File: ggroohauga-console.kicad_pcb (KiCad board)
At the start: 2 copper layers, 95 x 31 mm, 6 parts

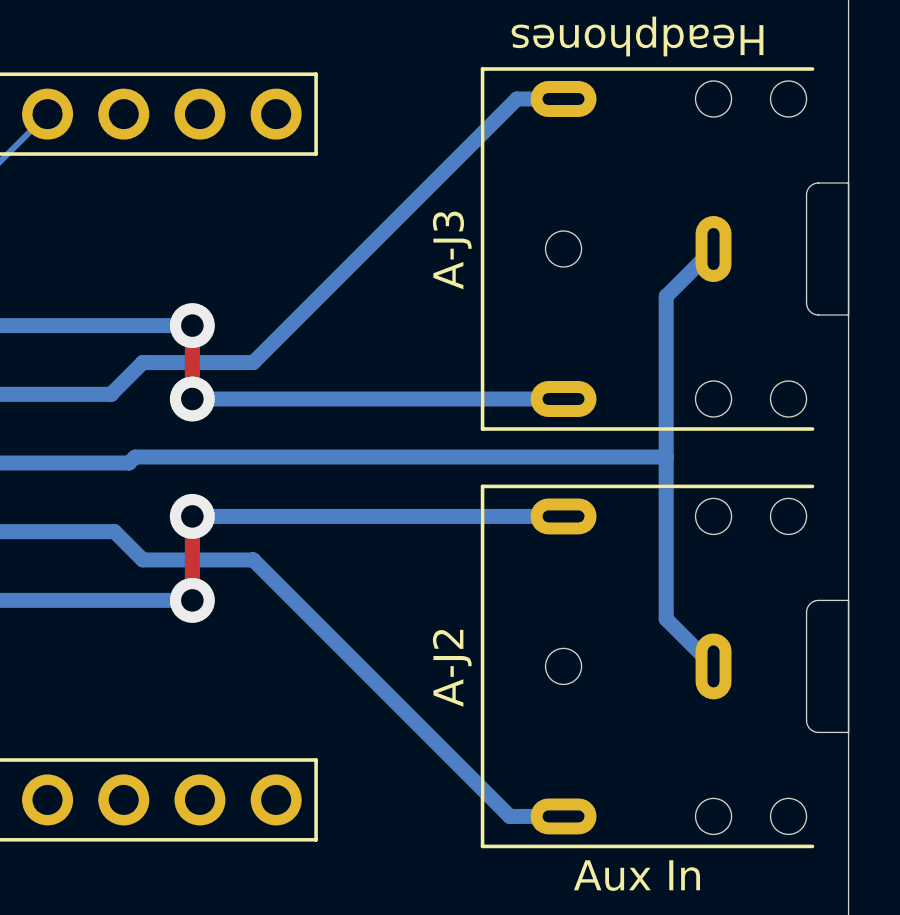
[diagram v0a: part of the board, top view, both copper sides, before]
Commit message: Fix component references for audio jacks
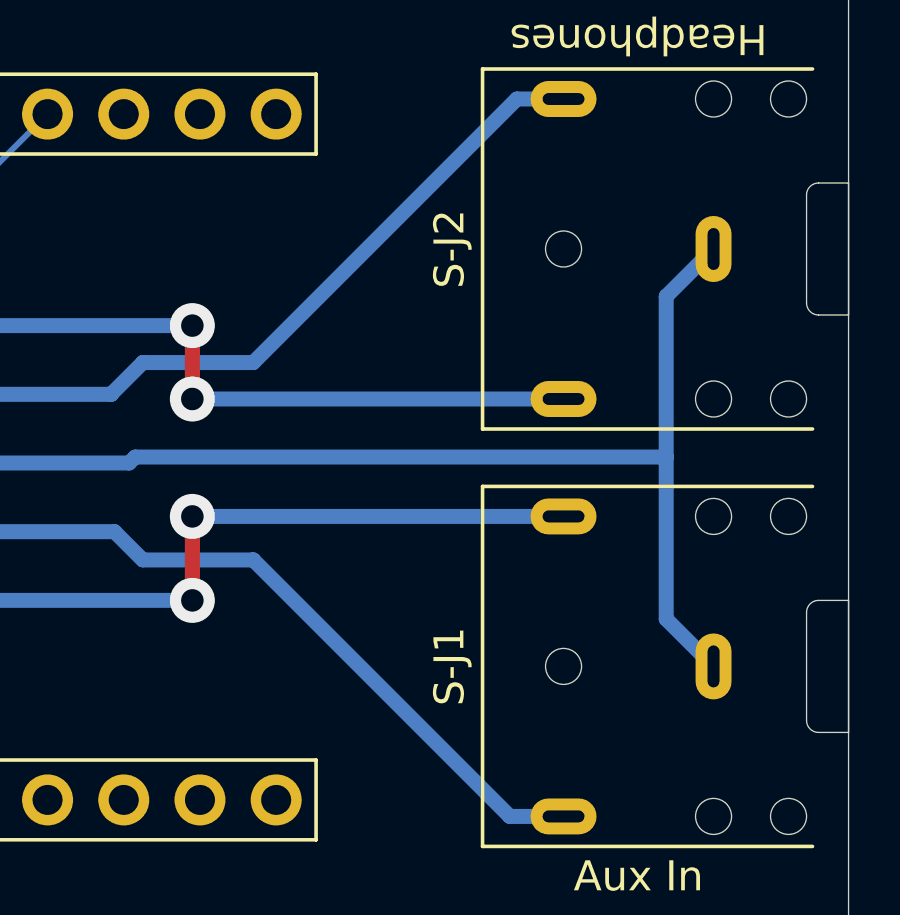
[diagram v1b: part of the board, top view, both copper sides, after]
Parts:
- renumbered A-J2 to S-J1, A-J3 to S-J2
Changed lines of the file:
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@@
 		(descr "TRS 3.5mm, horizontal, through-hole, https://www.cuidevices.com/product/resource/pdf/sj1-352xn.pdf")
 		(tags "TRS audio jack stereo horizontal")
-		(property "Reference" "A-J2"
+		(property "Reference" "S-J1"
 			(at 0 -8.8 90)
 			(layer "F.SilkS")
@@
 		(descr "TRS 3.5mm, horizontal, through-hole, https://www.cuidevices.com/product/resource/pdf/sj1-352xn.pdf")
 		(tags "TRS audio jack stereo horizontal")
-		(property "Reference" "A-J3"
+		(property "Reference" "S-J2"
 			(at 0 -8.8 90)
 			(layer "F.SilkS")

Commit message: Add "music with rocks in" image
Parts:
- added MUSICWITHROCKSIN: LOGO, LOGO, B.Cu at (81.3, 64.5)

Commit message: Fix thin lines in image
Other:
- board text added: "https://github.com/nomis/ggroohauga-pcb (console)"
- board text added: "urn:oid:1.3.6.1.4.1.39777.1.3.1.2.3"
- board text removed: "urn:oid:1.3.6.1.4.1.39777.1.3.1.2.3 https://github.com/nomis/ggroohauga-pcb (console)"

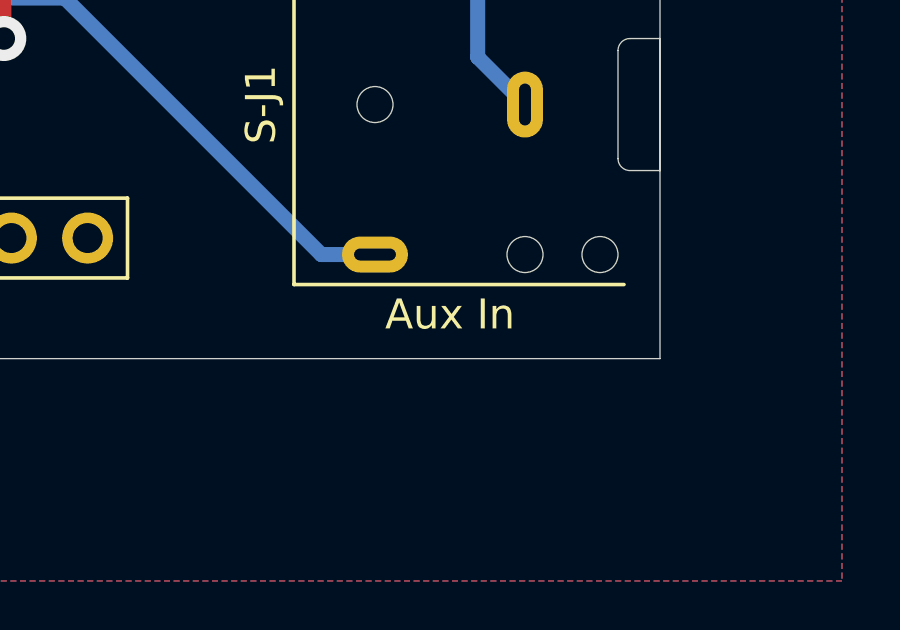
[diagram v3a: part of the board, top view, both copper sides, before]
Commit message: Rename "Aux In" to "Aux Input" and document 3.5mm audio sockets
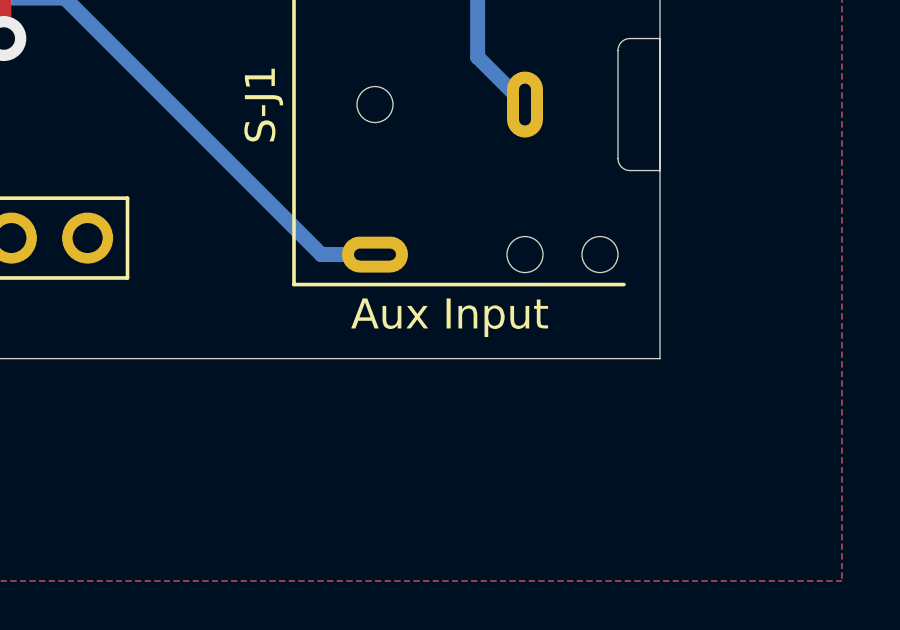
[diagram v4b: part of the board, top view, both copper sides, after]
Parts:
- S-J1: value Aux In -> Aux Input
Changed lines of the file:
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@@
 			)
 		)
-		(property "Value" "Aux In"
+		(property "Value" "Aux Input"
 			(at -7 -2.5 0)
 			(unlocked yes)

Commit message: Fix GPIO assignments
Stop using GPIO 14 because the pull-up isn't working reliably on my LOLIN
S3 board even when floating and I don't have another one to test it with.

Don't use GPIO 35 on the DevKitC-1 board because that conflicts with the
Octal PSRAM.
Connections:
- S3R1 pad 13: /Common/GPIO_L48_C35_M36/CON_ANNOUNCE -> unconnected-(S3R1-Pin_13-Pad13)
- S3R1 pad 14: GND -> unconnected-(S3R1-Pin_14-Pad14)
- S3R1 pad 15: GND -> /Common/GPIO_L21_C21_M21/AMP_DETECT
- S3R1 pad 16: /Common/GPIO_L14_C48_M33/AMP_DETECT -> GND
- S3R1 pad 7: GND -> /Common/GPIO_L41_C41_M42/CON_ANNOUNCE
- S3R1 pad 9: GND -> unconnected-(S3R1-Pin_9-Pad9)
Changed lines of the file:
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@@
 	(net 29 "/Common/GPIO_L8_C8_M10{slash}AMP_POWER_IN")
 	(net 30 "/Common/GPIO_L9_C9_M13{slash}AMP_TX")
-	(net 31 "/Common/GPIO_L14_C48_M33{slash}AMP_DETECT")
-	(net 32 "/Common/GPIO_L10_C10_M14{slash}AMP_RX")
-	(net 33 "/Common/GPIO_L48_C35_M36{slash}CON_ANNOUNCE")
-	(net 34 "/Common/GPIO_L13_C47_M26{slash}AMP_ANNOUNCE")
-	(net 35 "/Common/GPIO_L4_C4_M2{slash}CON_RX")
-	(net 36 "/Common/CON_POWER_OUT")
-	(net 37 "/Common/GPIO_L6_C6_M4{slash}CON_TX")
-	(net 38 "/Common/GPIO_L17_C17_M8{slash}CON_DETECT")
-	(net 39 "/Common/GPIO_L40_C40_M41{slash}CON_POWER_OUT")
-	(net 40 "GND")
+	(net 31 "/Common/GPIO_L10_C10_M14{slash}AMP_RX")
+	(net 32 "/Common/GPIO_L13_C47_M26{slash}AMP_ANNOUNCE")
+	(net 33 "/Common/GPIO_L4_C4_M2{slash}CON_RX")
+	(net 34 "/Common/CON_POWER_OUT")
+	(net 35 "/Common/GPIO_L6_C6_M4{slash}CON_TX")
+	(net 36 "/Common/GPIO_L17_C17_M8{slash}CON_DETECT")
+	(net 37 "/Common/GPIO_L40_C40_M41{slash}CON_POWER_OUT")
+	(net 38 "GND")
+	(net 39 "/Common/GPIO_L21_C21_M21{slash}AMP_DETECT")
+	(net 40 "/Common/GPIO_L41_C41_M42{slash}CON_ANNOUNCE")
+	(net 41 "unconnected-(S3R1-Pin_14-Pad14)")
+	(net 42 "unconnected-(S3R1-Pin_9-Pad9)")
+	(net 43 "unconnected-(S3R1-Pin_13-Pad13)")
 	(footprint "Package_TO_SOT_SMD:SOT-23"
 		(layer "F.Cu")
@@
 			(layers "F.Cu" "F.Mask" "F.Paste")
 			(roundrect_rratio 0.25)
-			(net 39 "/Common/GPIO_L40_C40_M41{slash}CON_POWER_OUT")
+			(net 37 "/Common/GPIO_L40_C40_M41{slash}CON_POWER_OUT")
 			(pinfunction "G")
 			(pintype "passive")
@@
 			(layers "F.Cu" "F.Mask" "F.Paste")
 			(roundrect_rratio 0.25)
-			(net 36 "/Common/CON_POWER_OUT")
+			(net 34 "/Common/CON_POWER_OUT")
 			(pinfunction "D")
 			(pintype "passive")
@@
 			(layers "*.Cu" "*.Mask")
 			(remove_unused_layers no)
-			(net 40 "GND")
+			(net 38 "GND")
 			(pinfunction "Pin_1")
 			(pintype "passive")
@@
 			(layers "*.Cu" "*.Mask")
 			(remove_unused_layers no)
-			(net 40 "GND")
+			(net 40 "/Common/GPIO_L41_C41_M42{slash}CON_ANNOUNCE")
 			(pinfunction "Pin_7")
 			(pintype "passive")
@@
 			(layers "*.Cu" "*.Mask")
 			(remove_unused_layers no)
-			(net 39 "/Common/GPIO_L40_C40_M41{slash}CON_POWER_OUT")
+			(net 37 "/Common/GPIO_L40_C40_M41{slash}CON_POWER_OUT")
 			(pinfunction "Pin_8")
 			(pintype "passive")
@@
 			(layers "*.Cu" "*.Mask")
 			(remove_unused_layers no)
-			(net 40 "GND")
+			(net 42 "unconnected-(S3R1-Pin_9-Pad9)")
 			(pinfunction "Pin_9")
-			(pintype "passive")
+			(pintype "passive+no_connect")
 		)
 		(pad "10" thru_hole circle
@@
 			(layers "*.Cu" "*.Mask")
 			(remove_unused_layers no)
-			(net 33 "/Common/GPIO_L48_C35_M36{slash}CON_ANNOUNCE")
+			(net 43 "unconnected-(S3R1-Pin_13-Pad13)")
 			(pinfunction "Pin_13")
-			(pintype "passive")
+			(pintype "passive+no_connect")
 		)
 		(pad "14" thru_hole circle
@@
 			(layers "*.Cu" "*.Mask")
 			(remove_unused_layers no)
-			(net 40 "GND")
+			(net 41 "unconnected-(S3R1-Pin_14-Pad14)")
 			(pinfunction "Pin_14")
-			(pintype "passive")
+			(pintype "passive+no_connect")
 		)
 		(pad "15" thru_hole circle
@@
 			(layers "*.Cu" "*.Mask")
 			(remove_unused_layers no)
-			(net 40 "GND")
+			(net 39 "/Common/GPIO_L21_C21_M21{slash}AMP_DETECT")
 			(pinfunction "Pin_15")
 			(pintype "passive")
@@
 			(layers "*.Cu" "*.Mask")
 			(remove_unused_layers no)
-			(net 31 "/Common/GPIO_L14_C48_M33{slash}AMP_DETECT")
+			(net 38 "GND")
 			(pinfunction "Pin_16")
 			(pintype "passive")
@@
 			(layers "*.Cu" "*.Mask")
 			(remove_unused_layers no)
-			(net 34 "/Common/GPIO_L13_C47_M26{slash}AMP_ANNOUNCE")
+			(net 32 "/Common/GPIO_L13_C47_M26{slash}AMP_ANNOUNCE")
 			(pinfunction "Pin_17")
 			(pintype "passive")
@@
 			(layers "*.Cu" "*.Mask")
 			(remove_unused_layers no)
-			(net 40 "GND")
+			(net 38 "GND")
 			(pintype "passive")
 			(solder_mask_margin 0.102)
@@
 			(layers "*.Cu" "*.Mask")
 			(remove_unused_layers no)
-			(net 40 "GND")
+			(net 38 "GND")
 			(pintype "passive")
 			(solder_mask_margin 0.102)
@@
 			(layers "*.Cu" "*.Mask")
 			(remove_unused_layers no)
-			(net 40 "GND")
+			(net 38 "GND")
 			(pintype "passive")
 			(solder_mask_margin 0.102)
@@
 			(layers "*.Cu" "*.Mask")
 			(remove_unused_layers no)
-			(net 34 "/Common/GPIO_L13_C47_M26{slash}AMP_ANNOUNCE")
+			(net 32 "/Common/GPIO_L13_C47_M26{slash}AMP_ANNOUNCE")
 			(pintype "passive")
 			(solder_mask_margin 0.102)
@@
 			(layers "*.Cu" "*.Mask")
 			(remove_unused_layers no)
-			(net 36 "/Common/CON_POWER_OUT")
+			(net 34 "/Common/CON_POWER_OUT")
 			(pintype "passive")
 			(solder_mask_margin 0.102)
@@
 			(layers "*.Cu" "*.Mask")
 			(remove_unused_layers no)
-			(net 35 "/Common/GPIO_L4_C4_M2{slash}CON_RX")
+			(net 33 "/Common/GPIO_L4_C4_M2{slash}CON_RX")
 			(pintype "passive")
 			(solder_mask_margin 0.102)
@@
 			(layers "*.Cu" "*.Mask")
 			(remove_unused_layers no)
-			(net 37 "/Common/GPIO_L6_C6_M4{slash}CON_TX")
+			(net 35 "/Common/GPIO_L6_C6_M4{slash}CON_TX")
 			(pintype "passive")
 			(solder_mask_margin 0.102)
@@
 			(layers "*.Cu" "*.Mask")
 			(remove_unused_layers no)
-			(net 38 "/Common/GPIO_L17_C17_M8{slash}CON_DETECT")
+			(net 36 "/Common/GPIO_L17_C17_M8{slash}CON_DETECT")
 			(pintype "passive")
 			(solder_mask_margin 0.102)
@@
 			(layers "*.Cu" "*.Mask")
 			(remove_unused_layers no)
-			(net 35 "/Common/GPIO_L4_C4_M2{slash}CON_RX")
+			(net 33 "/Common/GPIO_L4_C4_M2{slash}CON_RX")
 			(pinfunction "Pin_4")
 			(pintype "passive")
@@
 			(layers "*.Cu" "*.Mask")
 			(remove_unused_layers no)
-			(net 37 "/Common/GPIO_L6_C6_M4{slash}CON_TX")
+			(net 35 "/Common/GPIO_L6_C6_M4{slash}CON_TX")
 			(pinfunction "Pin_6")
 			(pintype "passive")
@@
 			(layers "*.Cu" "*.Mask")
 			(remove_unused_layers no)
-			(net 40 "GND")
+			(net 38 "GND")
 			(pinfunction "Pin_7")
 			(pintype "passive")
@@
 			(layers "*.Cu" "*.Mask")
 			(remove_unused_layers no)
-			(net 40 "GND")
+			(net 38 "GND")
 			(pinfunction "Pin_9")
 			(pintype "passive")
@@
 			(layers "*.Cu" "*.Mask")
 			(remove_unused_layers no)
-			(net 38 "/Common/GPIO_L17_C17_M8{slash}CON_DETECT")
+			(net 36 "/Common/GPIO_L17_C17_M8{slash}CON_DETECT")
 			(pinfunction "Pin_10")
 			(pintype "passive")
@@
 			(layers "*.Cu" "*.Mask")
 			(remove_unused_layers no)
-			(net 40 "GND")
+			(net 38 "GND")
 			(pinfunction "Pin_11")
 			(pintype "passive")
@@
 			(layers "*.Cu" "*.Mask")
 			(remove_unused_layers no)
-			(net 32 "/Common/GPIO_L10_C10_M14{slash}AMP_RX")
+			(net 31 "/Common/GPIO_L10_C10_M14{slash}AMP_RX")
 			(pinfunction "Pin_16")
 			(pintype "passive")
@@
 			(layers "*.Cu" "*.Mask")
 			(remove_unused_layers no)
-			(net 40 "GND")
+			(net 38 "GND")
 			(pinfunction "Pin_17")
 			(pintype "passive")
@@
 			(layers "*.Cu" "*.Mask")
 			(remove_unused_layers no)
-			(net 40 "GND")
+			(net 38 "GND")
 			(pinfunction "Pin_18")
 			(pintype "passive")
@@
 		(width 0.2)
 		(layer "B.Cu")
-		(net 34)
+		(net 32)
 	)
 	(segment
@@
 		(width 0.2)
 		(layer "B.Cu")
-		(net 34)
+		(net 32)
 	)
 	(segment
@@
 		(width 0.2)
 		(layer "B.Cu")
-		(net 34)
+		(net 32)
 	)
 	(segment
@@
 		(width 0.2)
 		(layer "B.Cu")
-		(net 34)
+		(net 32)
 	)
 	(segment
@@
 		(width 0.2)
 		(layer "B.Cu")
-		(net 34)
+		(net 32)
 	)
 	(segment
@@
 		(width 0.2)
 		(layer "B.Cu")
-		(net 35)
+		(net 33)
 	)
 	(segment
@@
 		(width 0.2)
 		(layer "B.Cu")
-		(net 35)
+		(net 33)
 	)
 	(segment
@@
 		(width 0.2)
 		(layer "B.Cu")
-		(net 35)
+		(net 33)
 	)
 	(segment
@@
 		(width 0.2)
 		(layer "B.Cu")
-		(net 35)
+		(net 33)
 	)
 	(segment
@@
 		(width 0.2)
 		(layer "B.Cu")
-		(net 35)
+		(net 33)
 	)
 	(segment
@@
 		(width 0.2)
 		(layer "B.Cu")
-		(net 35)
+		(net 33)
 	)
 	(segment
@@
 		(width 0.2)
 		(layer "F.Cu")
-		(net 36)
+		(net 34)
 	)
 	(segment
@@
 		(width 0.2)
 		(layer "F.Cu")
-		(net 36)
+		(net 34)
 	)
 	(segment
@@
 		(width 0.2)
 		(layer "F.Cu")
-		(net 36)
+		(net 34)
 	)
 	(segment
@@
 		(width 0.2)
 		(layer "F.Cu")
-		(net 36)
+		(net 34)
 	)
 	(segment
@@
 		(width 0.2)
 		(layer "F.Cu")
-		(net 36)
+		(net 34)
 	)
 	(segment
@@
 		(width 0.2)
 		(layer "F.Cu")
-		(net 36)
+		(net 34)
 	)
 	(segment
@@
 		(width 0.2)
 		(layer "B.Cu")
-		(net 37)
+		(net 35)
 	)
 	(segment
@@
 		(width 0.2)
 		(layer "B.Cu")
-		(net 37)
+		(net 35)
 	)
 	(segment
@@
 		(width 0.2)
 		(layer "B.Cu")
-		(net 37)
+		(net 35)
 	)
 	(segment
@@
 		(width 0.2)
 		(layer "B.Cu")
-		(net 37)
+		(net 35)
 	)
 	(segment
@@
 		(width 0.2)
 		(layer "B.Cu")
-		(net 37)
+		(net 35)
 	)
 	(segment
@@
 		(width 0.2)
 		(layer "B.Cu")
-		(net 37)
+		(net 35)
 	)
 	(segment
@@
 		(width 0.2)
 		(layer "B.Cu")
-		(net 37)
+		(net 35)
 	)
 	(segment
@@
 		(width 0.2)
 		(layer "B.Cu")
-		(net 38)
+		(net 36)
 	)
 	(segment
@@
 		(width 0.2)
 		(layer "B.Cu")
-		(net 38)
+		(net 36)
 	)
 	(segment
@@
 		(width 0.2)
 		(layer "B.Cu")
-		(net 38)
+		(net 36)
 	)
 	(segment
@@
 		(width 0.2)
 		(layer "B.Cu")
-		(net 38)
+		(net 36)
 	)
 	(segment
@@
 		(width 0.2)
 		(layer "B.Cu")
-		(net 38)
+		(net 36)
 	)
 	(segment
@@
 		(width 0.2)
 		(layer "B.Cu")
-		(net 38)
+		(net 36)
 	)
 	(segment
@@
 		(width 0.2)
 		(layer "B.Cu")
-		(net 38)
+		(net 36)
 	)
 	(segment
@@
 		(width 0.2)
 		(layer "F.Cu")
-		(net 39)
+		(net 37)
 	)
 	(segment
@@
 		(width 0.2)
 		(layer "F.Cu")
-		(net 39)
+		(net 37)
 	)
 	(zone
-		(net 40)
+		(net 38)
 		(net_name "GND")
 		(layers "F.Cu" "B.Cu")
